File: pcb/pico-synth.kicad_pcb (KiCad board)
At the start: 2 copper layers, 55.8 x 77.7 mm, 45 parts, among them J1 JST XH 2P, J2 JST XH 5P, J3 JST XH 4P, J4 JST XH 3P, SW1 Rotary_Encoder_Switch, U1 Pico, U2 6N137, U3 24LC512, U4 MCP4822, U5 LTC1044, U6 TL071, U7 TL072

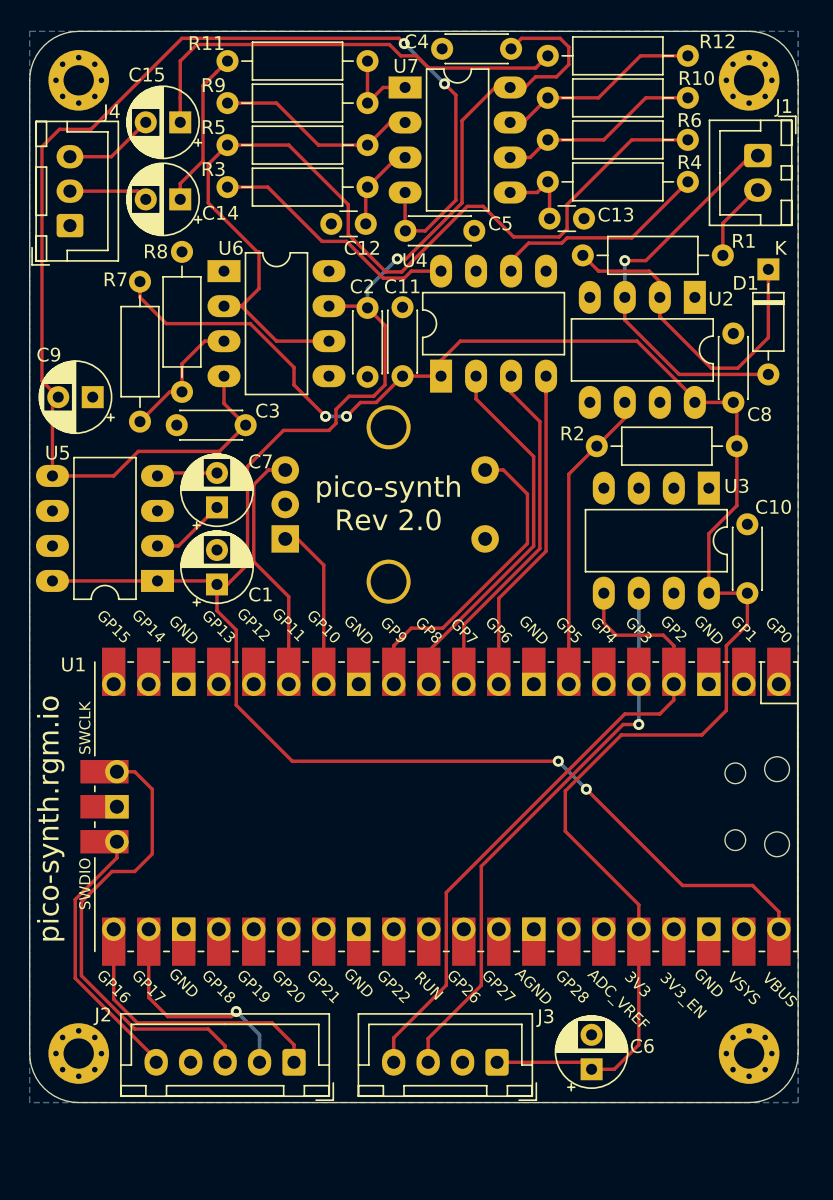
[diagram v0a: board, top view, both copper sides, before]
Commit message: new hardware revision: 2.1
this adds a two leds, for output monitoring
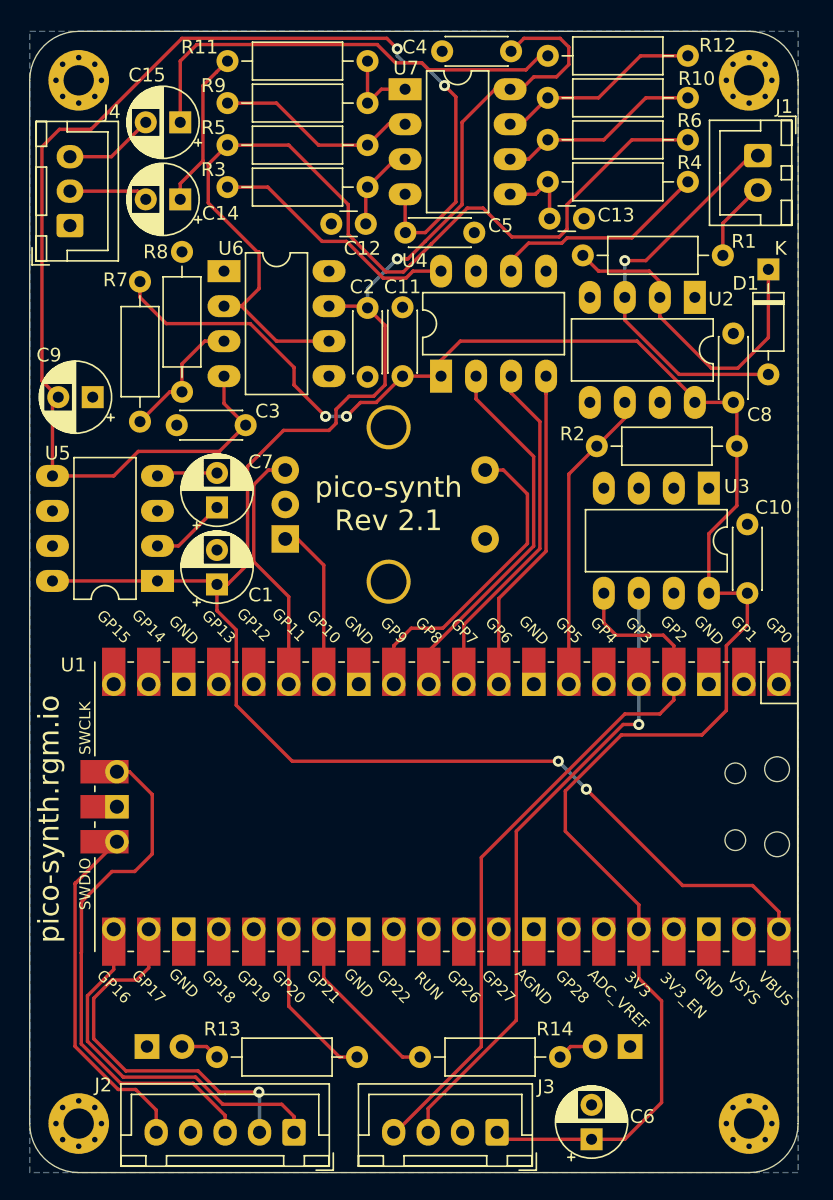
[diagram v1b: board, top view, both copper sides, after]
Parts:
- added D2: LED, LED_THT:LED_D3.0mm, B.Cu at (161.9, 134.5)
- added D3: LED, LED_THT:LED_D3.0mm, B.Cu at (126.9, 134.5)
- added R13: 18k, Resistor_THT:R_Axial_DIN0207_L6.3mm_D2.5mm_P10.16mm_Horizontal, F.Cu at (142.1, 135.3)
- added R14: 18k, Resistor_THT:R_Axial_DIN0207_L6.3mm_D2.5mm_P10.16mm_Horizontal, F.Cu at (146.7, 135.3)
- moved J2 5.08 mm to (137.5, 140.7)
- moved J3 5.08 mm to (152.3, 140.7)
- moved C6 5.08 mm to (159.1, 141.2)
- moved H3 5.08 mm to (121.9, 140.1)
- moved H4 5.08 mm to (170.6, 140.1)
- moved C4 0.18 mm to (153.3, 62.3)
- moved C5 0.13 mm to (150.6, 75.4)
- moved U7 0.13 mm to (145.6, 65.0)
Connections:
- U1 pad 26: Net-(U1-Pad26) -> LED2
- U1 pad 27: Net-(U1-Pad27) -> LED1
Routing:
- net LED1: track 0.00 -> 12.9 mm
- net LED2: track 0.00 -> 12.1 mm
- net DBG_RX: track 16.4 -> 27.2 mm
- net +3V3: track 126.1 -> 133.0 mm
- net DBG_TX: track 20.8 -> 27.3 mm
- net DBG_SWDIO: track 19.7 -> 25.6 mm
- net SDA: track 49.1 -> 54.2 mm
- net SCL: track 41.0 -> 46.1 mm
- net DBG_SWCLK: track 33.4 -> 38.3 mm
- net Net-(D3-Pad2): track 0.00 -> 2.86 mm
- net Net-(D2-Pad2): track 0.00 -> 2.86 mm
- net Net-(C12-Pad1): track 6.52 -> 7.05 mm
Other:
- board size 55.8 x 77.7 mm -> 55.8 x 82.8 mm
- board text added: "pico-synth Rev 2.1"
- board text removed: "pico-synth Rev 2.0"

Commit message: pcb: upgrade to kicad 6
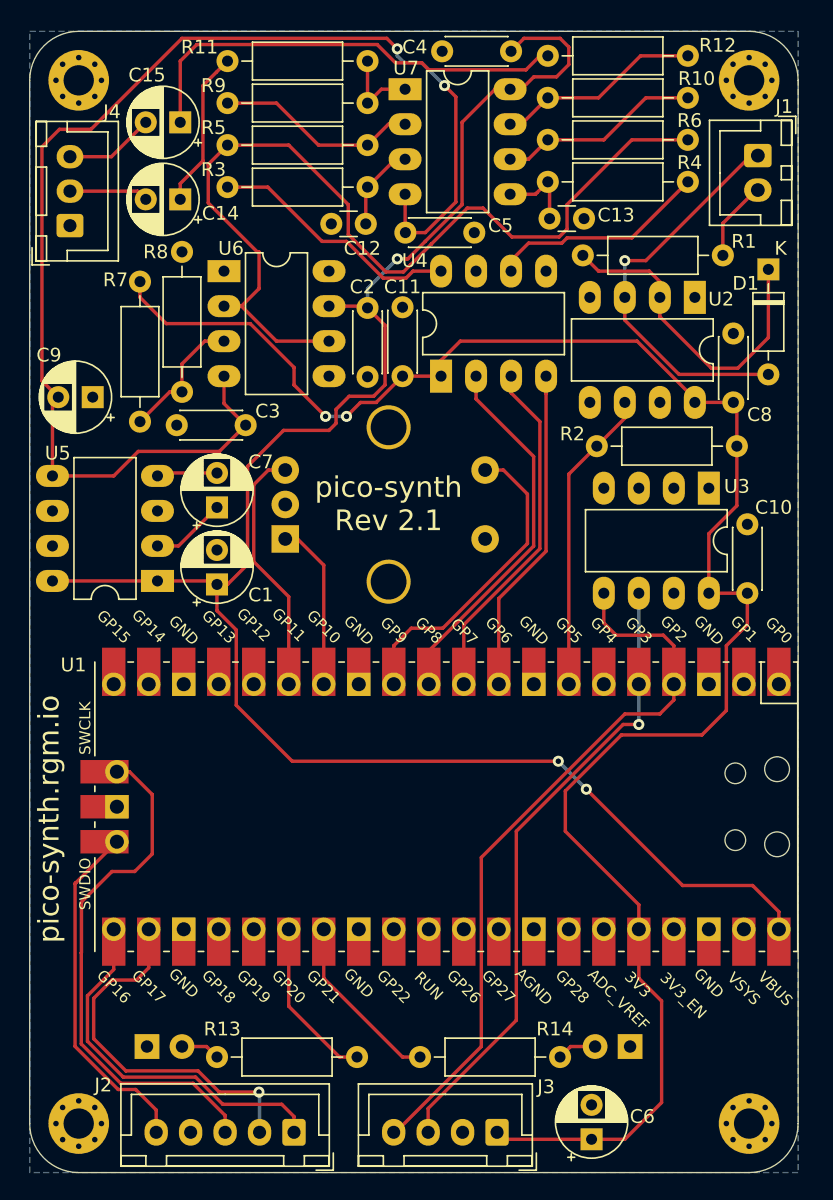
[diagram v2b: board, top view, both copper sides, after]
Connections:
- U1 pad 1: Net-(U1-Pad1) -> unconnected-(U1-Pad1)
- U1 pad 16: Net-(U1-Pad16) -> unconnected-(U1-Pad16)
- U1 pad 17: Net-(U1-Pad17) -> unconnected-(U1-Pad17)
- U1 pad 19: Net-(U1-Pad19) -> unconnected-(U1-Pad19)
- U1 pad 2: Net-(U1-Pad2) -> unconnected-(U1-Pad2)
- U1 pad 20: Net-(U1-Pad20) -> unconnected-(U1-Pad20)
- U1 pad 24: Net-(U1-Pad24) -> unconnected-(U1-Pad24)
- U1 pad 25: Net-(U1-Pad25) -> unconnected-(U1-Pad25)
- U1 pad 29: Net-(U1-Pad29) -> unconnected-(U1-Pad29)
- U1 pad 30: Net-(U1-Pad30) -> unconnected-(U1-Pad30)
- U1 pad 31: Net-(U1-Pad31) -> unconnected-(U1-Pad31)
- U1 pad 32: Net-(U1-Pad32) -> unconnected-(U1-Pad32)
- U1 pad 34: Net-(U1-Pad34) -> unconnected-(U1-Pad34)
- U1 pad 35: Net-(U1-Pad35) -> unconnected-(U1-Pad35)
- U1 pad 37: Net-(U1-Pad37) -> unconnected-(U1-Pad37)
- U1 pad 39: Net-(U1-Pad39) -> unconnected-(U1-Pad39)
- U1 pad 6: Net-(U1-Pad6) -> unconnected-(U1-Pad6)
- U2 pad 1: (no net) -> unconnected-(U2-Pad1)
- U2 pad 7: (no net) -> unconnected-(U2-Pad7)
- U5 pad 6: (no net) -> unconnected-(U5-Pad6)
- U5 pad 7: (no net) -> unconnected-(U5-Pad7)
- U6 pad 1: (no net) -> unconnected-(U6-Pad1)
- U6 pad 5: (no net) -> unconnected-(U6-Pad5)
- U6 pad 8: (no net) -> unconnected-(U6-Pad8)
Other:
- net class Default removed

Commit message: pcb: added new revision 2.2
trying to avoid using dc-dc charge pump
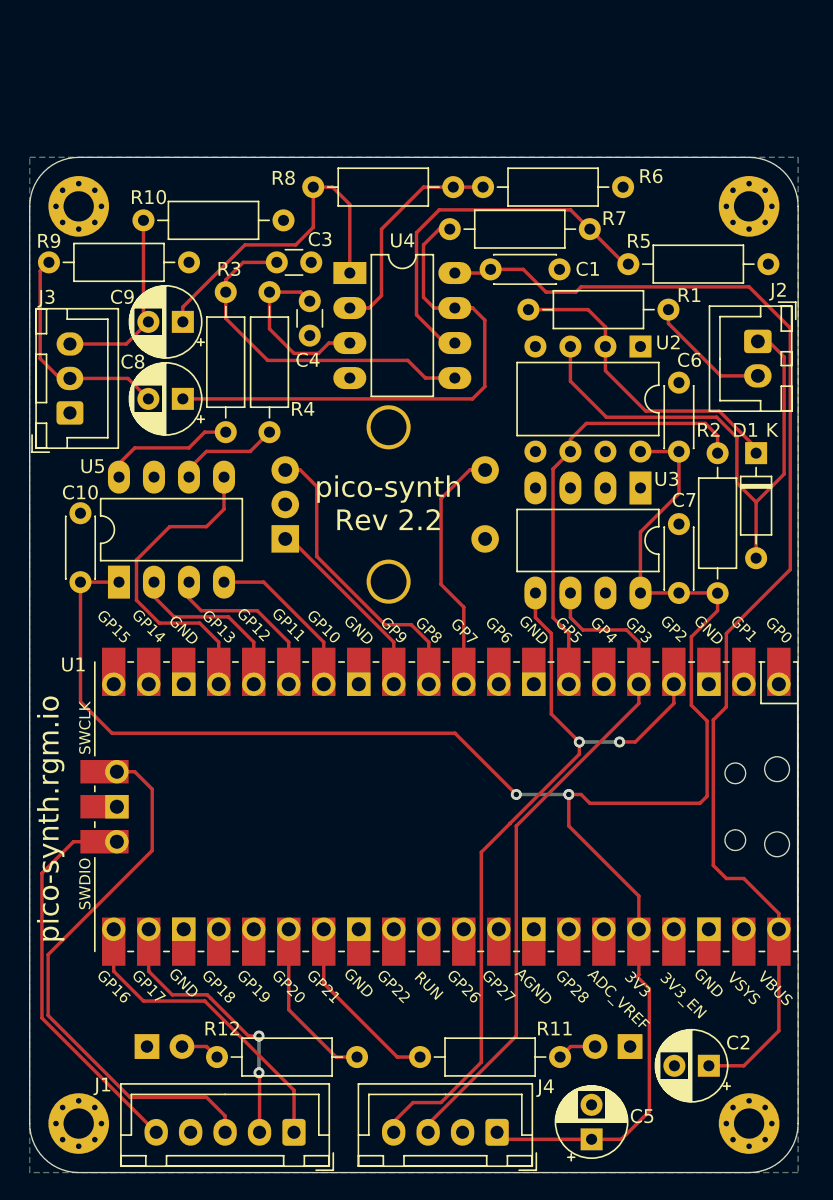
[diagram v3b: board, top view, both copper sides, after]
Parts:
- removed the C1 at (132.0, 101.0)
- removed C14, C15: 10u, Capacitor_THT:CP_Radial_D5.0mm_P2.50mm
- removed the C3 at (129.0, 89.4)
- removed the C4 at (153.3, 62.3)
- removed the C5 at (150.6, 75.4)
- removed the C7 at (132.0, 95.4)
- removed the R11 at (132.7, 63.0)
- removed the R12 at (156.0, 62.6)
- removed the R7 at (126.4, 79.0)
- removed the R8 at (129.4, 87.0)
- removed REF**: OSHW-Symbol_6.7x6mm_SilkScreen, Symbol:OSHW-Symbol_6.7x6mm_SilkScreen
- removed the U5 at (127.6, 100.7)
- removed U6: TL071, Package_DIP:DIP-8_W7.62mm_LongPads
- removed U7: TL072, Package_DIP:DIP-8_W7.62mm_LongPads
- added C2: 10u, Capacitor_THT:CP_Radial_D5.0mm_P2.50mm, F.Cu at (167.6, 135.9)
- added C8: 10u, Capacitor_THT:CP_Radial_D5.0mm_P2.50mm, F.Cu at (129.5, 87.5)
- added R10: 10k, Resistor_THT:R_Axial_DIN0207_L6.3mm_D2.5mm_P10.16mm_Horizontal, F.Cu at (126.6, 74.5)
- added R9: 10k, Resistor_THT:R_Axial_DIN0207_L6.3mm_D2.5mm_P10.16mm_Horizontal, F.Cu at (119.8, 77.6)
- added U4: TLV272, Package_DIP:DIP-8_W7.62mm_LongPads, F.Cu at (141.6, 78.4)
- U2: footprint Package_DIP:DIP-8_W7.62mm_LongPads -> Package_DIP:DIP-8_W7.62mm
- moved R5 40.2 mm to (172.0, 77.7), turned to 180 degrees
- moved U5 27.7 mm to (124.8, 100.8)
- moved C10 27.7 mm to (122.0, 100.8)
- moved R4 21.7 mm to (135.8, 79.8), turned to -90 degrees
- moved C4 18.4 mm to (138.7, 80.4), turned to -90 degrees
- moved R8 18.2 mm to (138.9, 72.1)
- moved J3 13.6 mm to (121.3, 88.5)
- moved J2 13.5 mm to (171.2, 83.3)
- moved D1 13.4 mm to (171.1, 91.4)
- moved R3 12.8 mm to (132.6, 79.8), turned to -90 degrees
- moved R7 10.9 mm to (148.8, 75.2), turned to 0 degrees
- moved R2 10.8 mm to (168.3, 101.6), turned to 90 degrees
- moved C1 9.36 mm to (151.8, 78.1), turned to 0 degrees
- moved H1 9.14 mm to (121.9, 73.5)
- moved H2 9.14 mm to (170.6, 73.5)
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- renumbered C2 to C1, C11 to C10, C12 to C3, C13 to C4, C6 to C5, C8 to C6, C10 to C7, J2 to J1, J1 to J2, J4 to J3, J3 to J4, R14 to R11, R13 to R12, R9 to R7, R10 to R8, U4 to U5
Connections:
- C9 pad 1: GND -> Net-(C9-Pad1)
- C9 pad 2: -5V -> Net-(C9-Pad2)
- J3 pad 3: Net-(C15-Pad2) -> Net-(C9-Pad2)
- R5 pad 1: VREF -> GND
- R6 pad 1: VREF -> GND
- R8 pad 1: Net-(R10-Pad1) -> Net-(C9-Pad1)
- U1 pad 10: SCK -> ENC_BT
- U1 pad 11: CS -> ENC_B
- U1 pad 12: ENC_BT -> ENC_A
- U1 pad 14: ENC_A -> SDI
- U1 pad 15: ENC_B -> SCK
- U1 pad 16: unconnected-(U1-Pad16) -> CS
- U1 pad 17: unconnected-(U1-Pad17) -> LDAC
- U1 pad 9: SDI -> unconnected-(U1-Pad9)
- U5 pad 5: GND -> LDAC
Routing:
- net -5V: track 94.6 -> 0.00 mm, vias 2 -> 0
- net VREF: track 68.3 -> 0.00 mm
- net +5V: track 132.7 -> 88.7 mm, vias 3 -> 0
- net Net-(C15-Pad1): track 32.8 -> 0.00 mm
- net Net-(C8-Pad1): track 6.19 -> 38.4 mm
- net Net-(C9-Pad1): track 0.00 -> 24.0 mm
- net LDAC: track 0.00 -> 23.4 mm
- net Net-(C3-Pad1): track 7.05 -> 25.4 mm
- net Net-(R10-Pad1): track 15.0 -> 0.00 mm
- net CS: track 27.2 -> 12.7 mm
- net Net-(C9-Pad2): track 0.00 -> 13.9 mm
- net SDI: track 25.2 -> 12.1 mm
- net SCK: track 25.5 -> 12.8 mm
- net Net-(R5-Pad2): track 14.8 -> 27.3 mm
- net Net-(C14-Pad1): track 11.5 -> 0.00 mm
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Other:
- board size 55.8 x 82.8 mm -> 55.8 x 73.7 mm
- board text added: "pico-synth Rev 2.2"
- board text removed: "pico-synth Rev 2.1"

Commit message: wip
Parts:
- U3, U4, U5: footprint Package_DIP:DIP-8_W7.62mm_LongPads -> Package_DIP:DIP-8_W7.62mm
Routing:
- net DBG_RX: track 20.0 -> 29.1 mm, vias 2 -> 0
